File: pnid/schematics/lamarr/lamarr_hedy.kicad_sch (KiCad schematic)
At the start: 102 parts

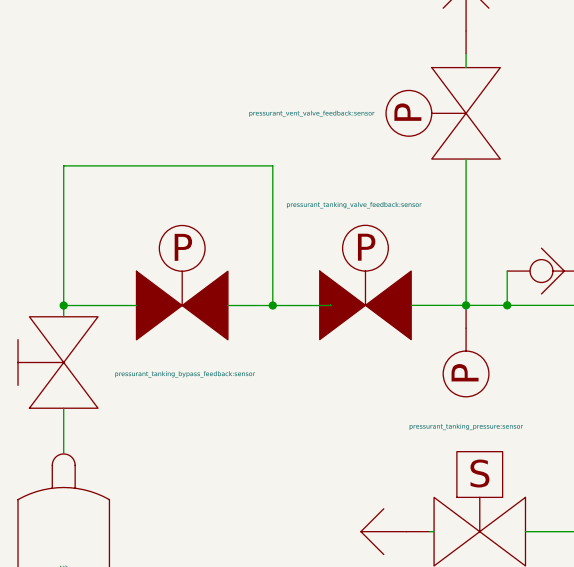
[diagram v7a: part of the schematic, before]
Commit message: added bypass solenoid to PnID
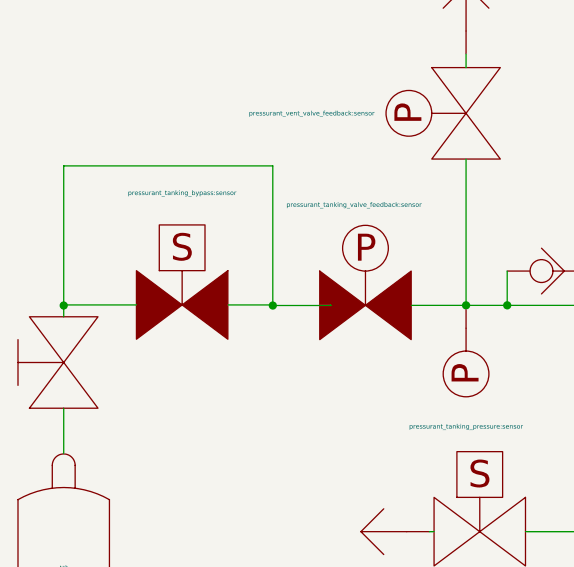
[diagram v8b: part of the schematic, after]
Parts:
- removed pressurant_tanking_bypass: pressurant_tanking_bypass_feedback:sensor, symbol PnID-Lib:Valve_Pneumatic
- added pressurant_tanking_bypass: pressurant_tanking_bypass:sensor, symbol PnID-Lib:Valve_Solenoid_NC
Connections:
- net at engine.~ (C): now also venturi1.~; no longer ox_venturi.~
- net at venturi1.~: now also fuel_main_valve.~, fuel_venturi_pressure.~; no longer engine.~ (C)
- net at dewar_needle_valve?.~: now also C2.~, C3.~; no longer C1.~
- net at dewar_manual_valve1.~, pressurant_tanking_valve_(A1).~: now also pressurant_tanking_bypass.~
- new net: engine.~ (C), ox_venturi.~
- new net: OX.~, ox_main_valve.~, ox_quick_connect.~
- new net: DewarOverPressureValve?.~, LOX.~, dewar_pressurize_solenoid.~
- new net: C1.~, dewar_needle_valve?.~
- new net: ox_pressurant_valve.~, ox_pressurant_vent_valve.~, pressurantPressureRegulator2.~
- new net: FUEL.~, fuel_main_valve.~, ox_quick_connect1.~
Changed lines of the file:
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@@
 	(wire
 		(pts
-			(xy 32.2151 56.1521) (xy 37.2007 56.1521)
+			(xy 32.2097 56.0889) (xy 37.1953 56.0889)
 		)
 		(stroke
@@
 	(wire
 		(pts
+			(xy 37.1953 56.0889) (xy 37.1953 56.1521)
+		)
+		(stroke
+			(width 0)
+			(type default)
+		)
+	)
+	(wire
+		(pts
 			(xy 65.278 81.28) (xy 78.486 81.28)
 		)
@@
 	(wire
 		(pts
+			(xy 13.9646 56.0889) (xy 13.9646 56.1521)
+		)
+		(stroke
+			(width 0)
+			(type default)
+		)
+	)
+	(wire
+		(pts
 			(xy 120.65 169.164) (xy 120.904 169.164)
 		)
@@
 	(wire
 		(pts
+			(xy 13.9646 56.1521) (xy 13.97 56.1521)
+		)
+		(stroke
+			(width 0)
+			(type default)
+		)
+	)
+	(wire
+		(pts
 			(xy 75.946 155.194) (xy 78.486 155.194)
 		)
@@
 	(wire
 		(pts
-			(xy 13.97 56.1521) (xy 22.0551 56.1521)
+			(xy 13.9646 56.0889) (xy 22.0497 56.0889)
 		)
 		(stroke
@@
 		(pts
 			(xy 189.23 113.284) (xy 200.66 113.284)
+		)
+		(stroke
+			(width 0)
+			(type default)
+		)
+	)
+	(wire
+		(pts
+			(xy 37.1953 56.1521) (xy 37.2007 56.1521)
 		)
 		(stroke
@@
 	)
 	(symbol
-		(lib_name "Valve_Pneumatic_3")
-		(lib_id "PnID-Lib:Valve_Pneumatic")
-		(at 27.1351 56.1521 0)
-		(mirror y)
+		(lib_name "Valve_Solenoid_NC_1")
+		(lib_id "PnID-Lib:Valve_Solenoid_NC")
+		(at 27.1297 56.0889 0)
 		(unit 1)
 		(exclude_from_sim no)
@@
 		(dnp no)
 		(property "Reference" "pressurant_tanking_bypass"
-			(at 27.1351 44.8999 0)
-			(effects
-				(font
-					(size 0.508 0.508)
-				)
-				(hide yes)
-			)
-		)
-		(property "Value" "pressurant_tanking_bypass_feedback:sensor"
-			(at 27.432 63.754 0)
+			(at 27.1297 44.8367 0)
+			(effects
+				(font
+					(size 0.508 0.508)
+				)
+				(hide yes)
+			)
+		)
+		(property "Value" "pressurant_tanking_bypass:sensor"
+			(at 27.1297 43.6429 0)
 			(effects
 				(font
@@
 		)
 		(property "Footprint" ""
-			(at 27.1351 56.1521 0)
+			(at 27.1297 56.0889 0)
 			(effects
 				(font
@@
 		)
 		(property "Datasheet" ""
-			(at 27.1351 56.1521 0)
+			(at 27.1297 56.0889 0)
 			(effects
 				(font
@@
 		)
 		(property "Description" ""
-			(at 27.1351 56.1521 0)
+			(at 27.1297 56.0889 0)
 			(effects
 				(font
@@
 		)
 		(property "Unit" "%"
-			(at 27.1351 56.1521 0)
+			(at 27.1297 56.0889 0)
 			(effects
 				(font
@@
 		)
 		(property "Action_Reference" " "
-			(at 27.1351 56.1521 0)
-			(effects
-				(font
+			(at 27.1297 56.0889 0)
+			(effects
+				(font
